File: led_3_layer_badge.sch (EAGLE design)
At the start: 59 parts, among them U1 ATMEGA168, U2 MCP73811, U3 AP34063, U4 PCA9952

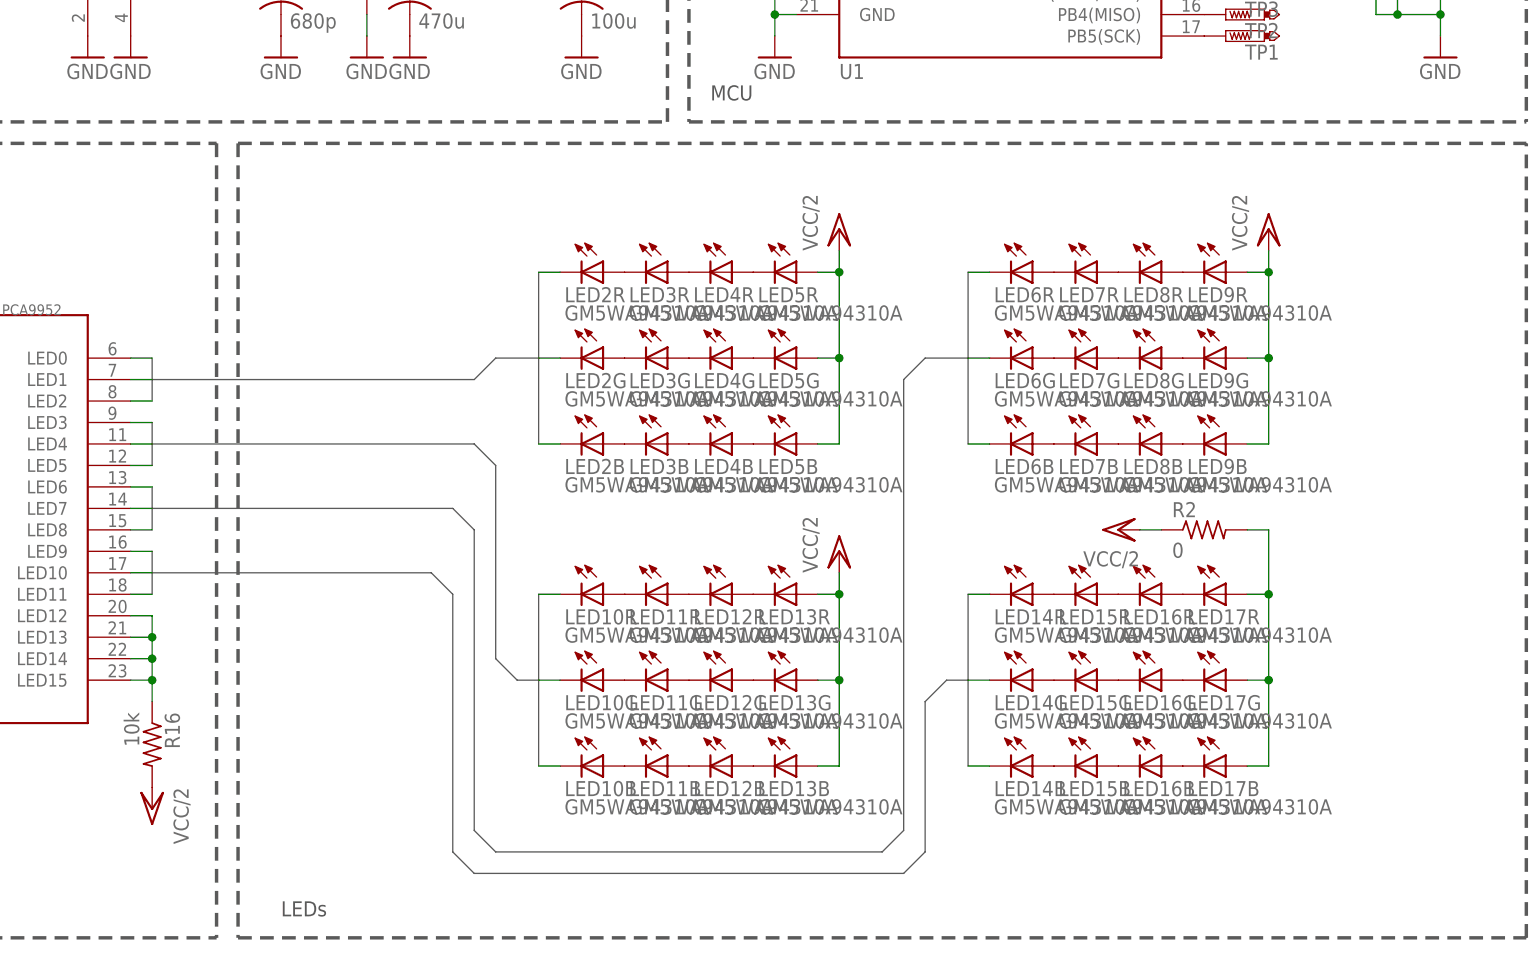
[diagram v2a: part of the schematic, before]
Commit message: added new concept image, found proper leds
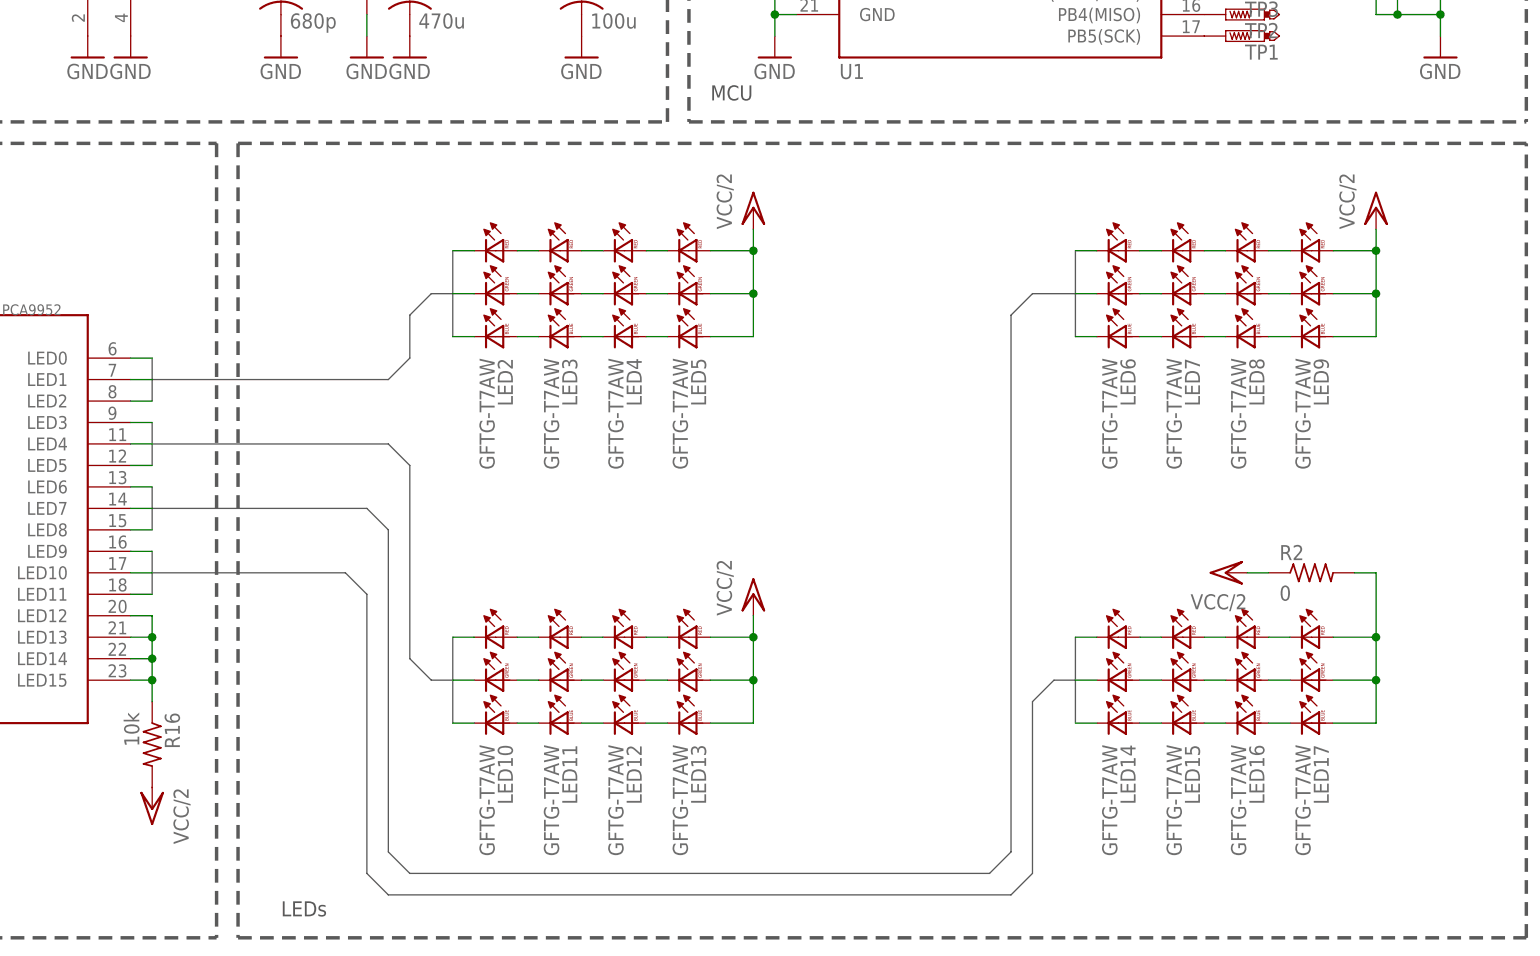
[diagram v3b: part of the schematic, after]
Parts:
- LED10, LED11, LED12, LED13, LED14, LED15, LED16, LED17, LED2, LED3, LED4, LED5, LED6, LED7, LED8, LED9: value GM5WA94310A -> GFTG-T7AW; device led:GM5WA94310A -> osram:GFTG-T7AW
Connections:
- net A0: now also LED2.RC; no longer LED2R.C
- net A1: now also LED2.GC; no longer LED2G.C
- net A2: now also LED2.BC; no longer LED2B.C
- net B0: now also LED10.RC; no longer LED10R.C
- net B1: now also LED10.GC; no longer LED10G.C
- net B2: now also LED10.BC; no longer LED10B.C
- net C0: now also LED6.RC; no longer LED6R.C
- net C1: now also LED6.GC; no longer LED6G.C
- net C2: now also LED6.BC; no longer LED6B.C
- net D0: now also LED14.RC; no longer LED14R.C
- net D1: now also LED14.GC; no longer LED14G.C
- net D2: now also LED14.BC; no longer LED14B.C
- net N$10: now also LED17.BA, LED17.GA, LED17.RA; no longer LED17B.A, LED17G.A, LED17R.A
- net N$12: now also LED6.BA, LED7.BC; no longer LED6R.A, LED7R.C
- net N$16: now also LED6.GA, LED7.GC; no longer LED6G.A, LED7G.C
- net N$17: now also LED6.RA, LED7.RC; no longer LED6B.A, LED7B.C
- net N$18: now also LED7.BA, LED8.BC; no longer LED8R.A, LED9R.C
- net N$19: now also LED7.GA, LED8.GC; no longer LED8G.A, LED9G.C
- net N$2: now also LED2.BA, LED3.BC; no longer LED2R.A, LED3R.C
- net N$20: now also LED7.RA, LED8.RC; no longer LED8B.A, LED9B.C
- net N$21: now also LED8.BA, LED9.BC; no longer LED7R.A, LED8R.C
- net N$22: now also LED8.GA, LED9.GC; no longer LED7G.A, LED8G.C
- net N$24: now also LED2.GA, LED3.GC; no longer LED2G.A, LED3G.C
- net N$25: now also LED2.RA, LED3.RC; no longer LED2B.A, LED3B.C
- net N$28: now also LED3.BA, LED4.BC; no longer LED4R.A, LED5R.C
- net N$29: now also LED3.GA, LED4.GC; no longer LED4G.A, LED5G.C
- net N$30: now also LED3.RA, LED4.RC; no longer LED4B.A, LED5B.C
- net N$31: now also LED4.BA, LED5.BC; no longer LED3R.A, LED4R.C
- net N$32: now also LED4.GA, LED5.GC; no longer LED3G.A, LED4G.C
- net N$33: now also LED4.RA, LED5.RC; no longer LED3B.A, LED4B.C
- net N$34: now also LED8.RA, LED9.RC; no longer LED7B.A, LED8B.C
- net N$35: now also LED10.BA, LED11.BC; no longer LED10R.A, LED11R.C
- net N$36: now also LED10.GA, LED11.GC; no longer LED10G.A, LED11G.C
- net N$37: now also LED10.RA, LED11.RC; no longer LED10B.A, LED11B.C
- net N$38: now also LED11.BA, LED12.BC; no longer LED12R.A, LED13R.C
- net N$39: now also LED11.GA, LED12.GC; no longer LED12G.A, LED13G.C
- net N$40: now also LED11.RA, LED12.RC; no longer LED12B.A, LED13B.C
- net N$41: now also LED12.BA, LED13.BC; no longer LED11R.A, LED12R.C
- net N$42: now also LED12.GA, LED13.GC; no longer LED11G.A, LED12G.C
- net N$43: now also LED12.RA, LED13.RC; no longer LED11B.A, LED12B.C
- net N$44: now also LED14.BA, LED15.BC; no longer LED14R.A, LED15R.C
- net N$45: now also LED14.GA, LED15.GC; no longer LED14G.A, LED15G.C
- net N$46: now also LED14.RA, LED15.RC; no longer LED14B.A, LED15B.C
- net N$47: now also LED15.BA, LED16.BC; no longer LED16R.A, LED17R.C
- net N$48: now also LED15.GA, LED16.GC; no longer LED16G.A, LED17G.C
- net N$49: now also LED15.RA, LED16.RC; no longer LED16B.A, LED17B.C
- net N$50: now also LED16.BA, LED17.BC; no longer LED15R.A, LED16R.C
- net N$51: now also LED16.GA, LED17.GC; no longer LED15G.A, LED16G.C
- net N$52: now also LED16.RA, LED17.RC; no longer LED15B.A, LED16B.C
- net VCC/2: now also LED13.BA, LED13.GA, LED13.RA, LED5.BA, LED5.GA, LED5.RA, LED9.BA, LED9.GA, LED9.RA; no longer LED13B.A, LED13G.A, LED13R.A, LED5B.A, LED5G.A, LED5R.A, LED9B.A, LED9G.A, LED9R.A
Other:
- moved on the sheet: R2

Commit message: revisions
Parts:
- removed JP1: (no value), sparkfun:M02-JST-2MM-SMT
- removed R11: 10k, rcl:R-US_R1206
- removed U1: ATMEGA168, sparkfun:ATMEGA168
- added IC1: TINY24/44/84, atmel:TINY24/44/84
- added TP6, TP7: PTR1B2,54, testpad:PTR1B2,54
- Q1: value (none) -> P-CH
- U3: value AP34063 -> MC33063A
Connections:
- removed net !SHDN: Q1.G, R8.1, U1.PD5(T1)
- removed net N$53: TP1.TP, U1.PB5(SCK)
- removed net N$54: TP2.TP, U1.PB4(MISO)
- removed net N$55: TP3.TP, U1.PB3(MOSI/OC2)
- removed net RX: U1.PD0(RXD)
- removed net TX: U1.PD1(TXD)
- new net MOSI: IC1.(ADC4/MISO/OC1B)PA5, TP1.TP
- net !OE: now also IC1.(ADC1/AIN0)PA1, Q1.G, R8.2; no longer R11.2, U1.PD4(XCK/T0)
- net !RST: now also IC1.(!RESET!)PB3; no longer U1.PC6(/RESET)
- net GND: now also IC1.GND, TP7.TP; no longer JP1.2, R8.2, U1.AGND, U1.GND@1, U1.GND@2
- net N$7: now also Q1.D; no longer Q1.S
- net S1: now also IC1.(ADC3)PA3; no longer U1.PD2(INT0)
- net S2: now also IC1.(ADC2/AIN1)PA2; no longer U1.PD3(INT1)
- net SCL: now also IC1.(ADC4/SCK/SCL)PA4, TP2.TP; no longer U1.PC5(ADC5/SCL)
- net SDA: now also IC1.(ADC6/MOSI/SDA/OC1A)PA6, TP3.TP; no longer U1.PC4(ADC4/SDA)
- net VCC: now also IC1.(ADC0/AREF)PA0, IC1.VCC, Q1.S, R8.1, TP6.TP; no longer JP1.1, Q1.D, R11.1, U1.AREF, U1.AVCC, U1.VCC@1, U1.VCC@2
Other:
- moved on the sheet: Q1, R12, R13, R8
